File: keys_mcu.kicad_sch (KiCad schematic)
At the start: 30 parts, among them J3 Conn_01x26_Socket, J5 Conn_ARM_JTAG_SWD_10, J6 Conn_02x03_Odd_Even, SW1 PWR, SW2 MUTE, SW2 Volume, SW3 PREV, SW4 PLAY_PAUSE, SW5 NEXT, U2 STM32G431CBUx, U7 SN65HVD230

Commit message: routing progress
Just nice to make some save points every now and again.
USB seems... ok?  Still need to check 3v3 or 5v on the power pullups,
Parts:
- added C2: 100nF, Capacitor_SMD:C_0603_1608Metric, symbol Device:C_Small
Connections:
- net +3V3: now also C2.2
- net GND: now also C2.1
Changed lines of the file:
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@@
   (junction (at 226.06 144.78) (diameter 0) (color 0 0 0 0)
+  )
+  (junction (at 203.2 63.5) (diameter 0) (color 0 0 0 0)
   )
   (junction (at 236.22 30.48) (diameter 0) (color 0 0 0 0)
@@
     (stroke (width 0) (type default))
   )
+  (wire (pts (xy 223.52 63.5) (xy 223.52 66.04))
+    (stroke (width 0) (type default))
+  )
   (wire (pts (xy 264.16 48.26) (xy 269.24 48.26))
     (stroke (width 0) (type default))
@@
     (stroke (width 0) (type default))
   )
+  (wire (pts (xy 218.44 63.5) (xy 223.52 63.5))
+    (stroke (width 0) (type default))
+  )
   (wire (pts (xy 68.58 121.92) (xy 63.5 121.92))
     (stroke (width 0) (type default))
@@
   )
   (wire (pts (xy 203.2 63.5) (xy 203.2 66.04))
+    (stroke (width 0) (type default))
+  )
+  (wire (pts (xy 213.36 63.5) (xy 203.2 63.5))
     (stroke (width 0) (type default))
   )
@@
         (path "/d0e4eaec-96cb-4a0e-a384-5b3e3f5f8d5d/7c81bc9d-f306-4c7f-90ce-10f7b22818e4"
           (reference "D3") (unit 1)
+        )
+      )
+    )
+  )
+  (symbol (lib_id "power:GND") (at 223.52 66.04 0) (unit 1)
+    (in_bom yes) (on_board yes) (dnp no) (fields_autoplaced)
+    (property "Reference" "#PWR047" (at 223.52 72.39 0)
+      (effects (font (size 1.27 1.27)) hide)
+    )
+    (property "Value" "GND" (at 223.52 71.12 0)
+      (effects (font (size 1.27 1.27)))
+    )
+    (property "Footprint" "" (at 223.52 66.04 0)
+      (effects (font (size 1.27 1.27)) hide)
+    )
+    (property "Datasheet" "" (at 223.52 66.04 0)
+      (effects (font (size 1.27 1.27)) hide)
+    )
+    (pin "1")
+    (instances
+      (project "das-kb4-bara2"
+        (path "/d0e4eaec-96cb-4a0e-a384-5b3e3f5f8d5d/7c81bc9d-f306-4c7f-90ce-10f7b22818e4"
+          (reference "#PWR047") (unit 1)
         )
       )
@@
         )
       )
+    )
+  )
+  (symbol (lib_id "Device:C_Small") (at 215.9 63.5 270) (unit 1)
+    (in_bom yes) (on_board yes) (dnp no)
+    (property "Reference" "C2" (at 214.6236 60.96 0)
+      (effects (font (size 1.27 1.27)) (justify right))
+    )
+    (property "Value" "100nF" (at 218.44 63.5 0)
+      (effects (font (size 1.27 1.27)) (justify right))
+    )
+    (property "Footprint" "Capacitor_SMD:C_0603_1608Metric" (at 215.9 63.5 0)
+      (effects (font (size 1.27 1.27)) hide)
+    )
+    (property "Datasheet" "~" (at 215.9 63.5 0)
+      (effects (font (size 1.27 1.27)) hide)
+    )
+    (property "MPN" "CC0603KRX7R9BB104 " (at 215.9 63.5 0)
+      (effects (font (size 1.27 1.27)) hide)
+    )
+    (property "lcsc#" "C14663" (at 215.9 63.5 0)
+      (effects (font (size 1.27 1.27)) hide)
+    )
+    (property "jlc-basic" "1" (at 215.9 63.5 0)
+      (effects (font (size 1.27 1.27)) hide)
+    )
+    (property "lcsc2#" "" (at 215.9 63.5 0)
+      (effects (font (size 1.27 1.27)) hide)
+    )
+    (pin "1")
+    (pin "2")
+    (instances
+      (project "r2022-12"
+        (path "/9d3292e9-89ed-435a-b615-fc52a41b2a3d/00000000-0000-0000-0000-00005e1ad3c1"
+          (reference "C2") (unit 1)
+        )
+      )
+      (project "das-kb4-bara2"
+        (path "/d0e4eaec-96cb-4a0e-a384-5b3e3f5f8d5d/f457a5c4-270e-459d-a4f0-150cf90e3909"
+          (reference "C1") (unit 1)
+        )
+        (path "/d0e4eaec-96cb-4a0e-a384-5b3e3f5f8d5d/7c81bc9d-f306-4c7f-90ce-10f7b22818e4"
+          (reference "C15") (unit 1)
+        )
+      )

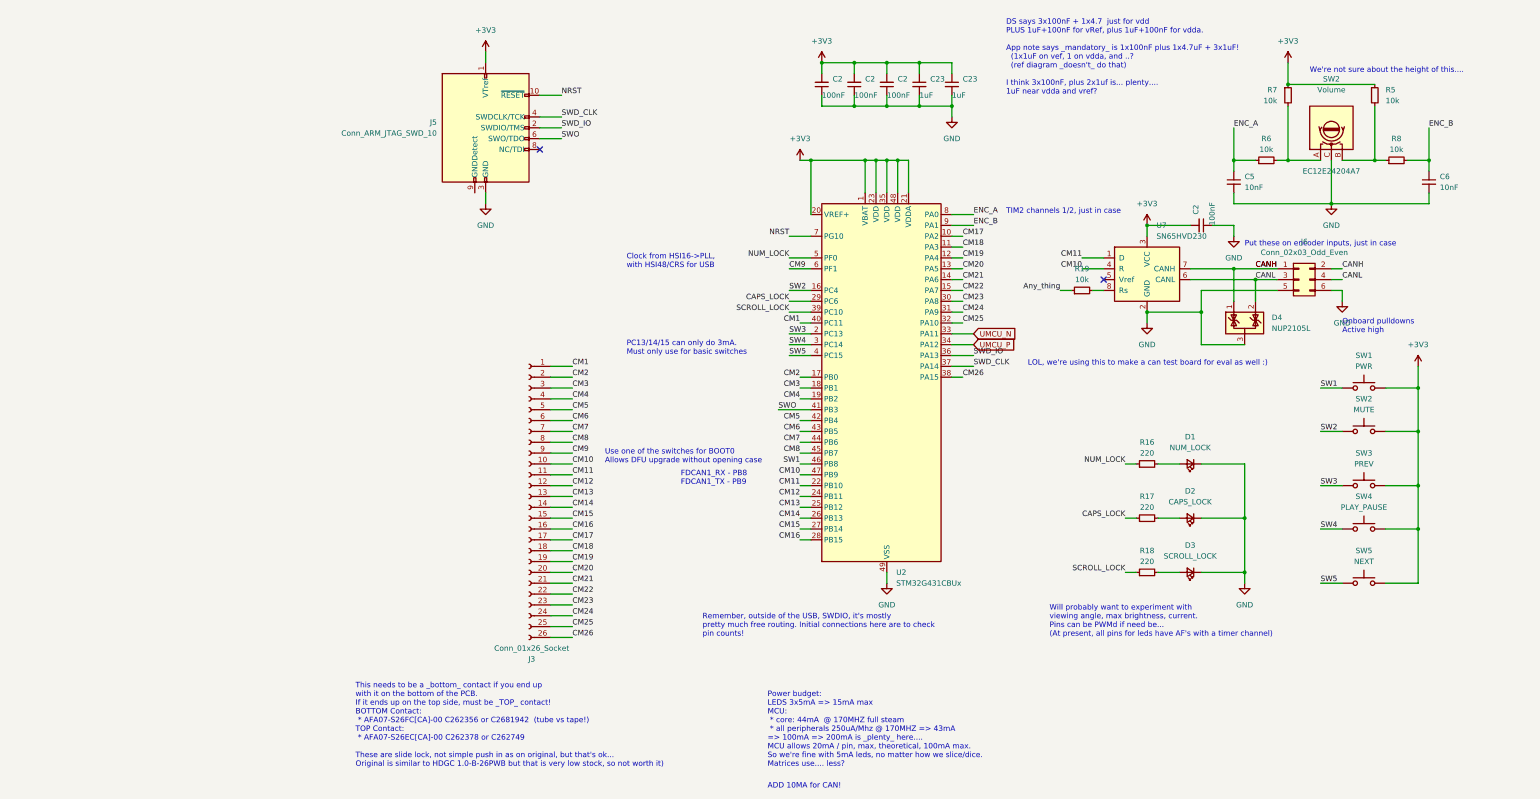
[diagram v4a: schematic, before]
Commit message: cleanup schematic, break out most of it
Broke it all out to the right places, now I can go and shuffle all the
labels to make it line up.  Thankfully we can just "freely" route the
keybaord matrix pins!
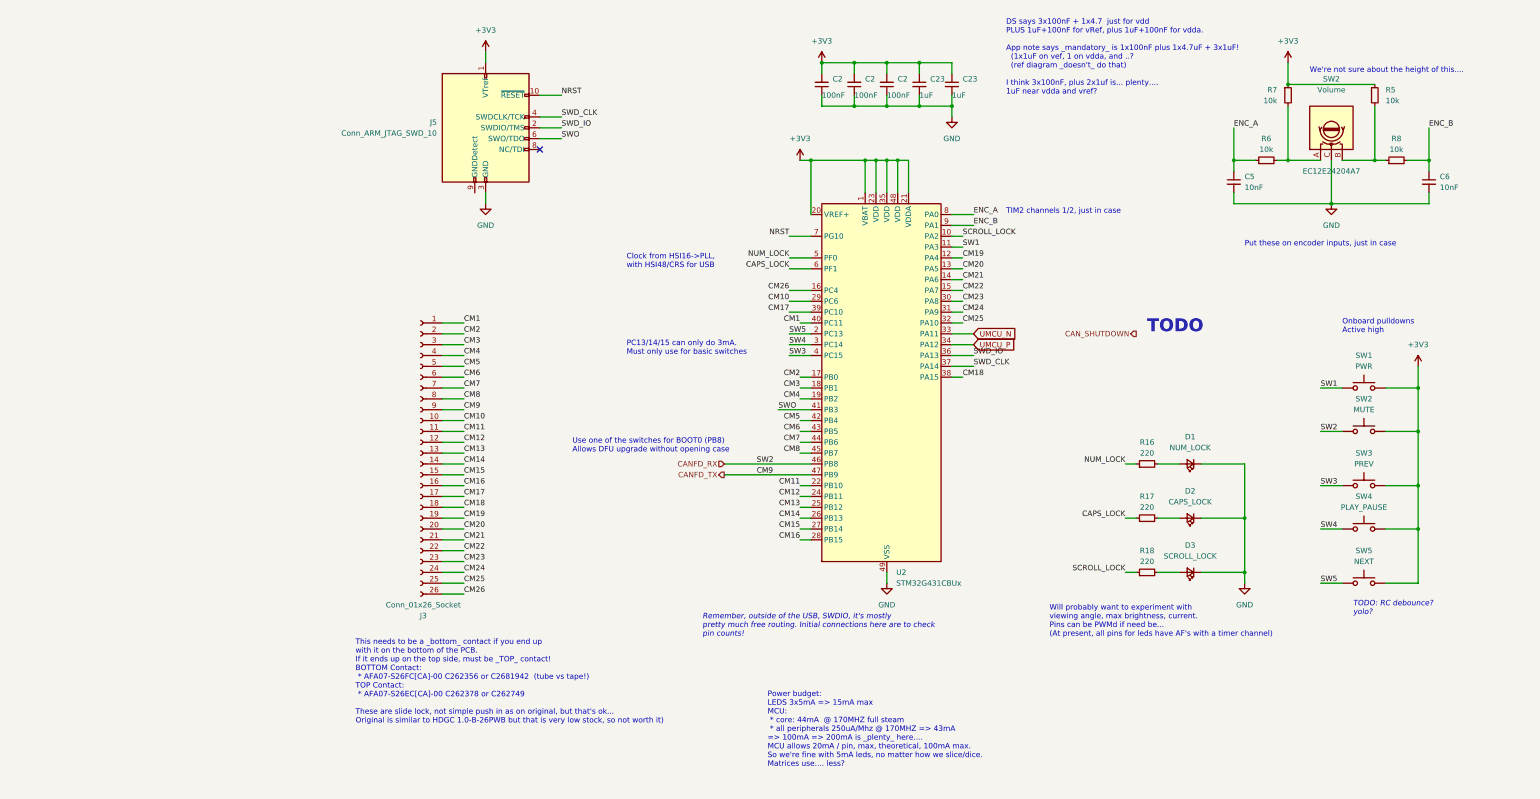
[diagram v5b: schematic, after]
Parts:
- removed C2: 100nF, Capacitor_SMD:C_0603_1608Metric, symbol Device:C_Small
- removed D4: NUP2105L, Package_TO_SOT_SMD:SOT-23, symbol Power_Protection:NUP2105L
- removed J6: Conn_02x03_Odd_Even, Connector_PinHeader_2.54mm:PinHeader_2x03_P2.54mm_Vertical, symbol Connector_Generic:Conn_02x03_Odd_Even
- removed R19: 10k, Resistor_SMD:R_0603_1608Metric, symbol Device:R_Small
- removed U7: SN65HVD230, Package_SO:SOIC-8_3.9x4.9mm_P1.27mm, symbol Interface_CAN_LIN:SN65HVD230
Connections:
- net CAPS_LOCK: now also U2.6 (PF1); no longer U2.29 (PC6)
- net CM10: now also U2.29 (PC6); no longer U2.47 (PB9)
- net CM17: now also U2.39 (PC10); no longer U2.10 (PA2)
- net CM18: now also U2.38 (PA15); no longer U2.11 (PA3)
- net CM26: now also U2.16 (PC4); no longer U2.38 (PA15)
- net SCROLL_LOCK: now also U2.10 (PA2); no longer U2.39 (PC10)
- net SW1: now also U2.11 (PA3); no longer U2.46 (PB8)
- net SW3: now also U2.4 (PC15); no longer U2.2 (PC13)
- net SW5: now also U2.2 (PC13); no longer U2.4 (PC15)
- net CM9 renamed CANFD_TX
- net CANFD_TX: now also U2.47 (PB9); no longer U2.6 (PF1)
- net SW2 renamed CANFD_RX
- net CANFD_RX: now also U2.46 (PB8); no longer U2.16 (PC4)
- no-connect marks 2 -> 1
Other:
- note added: "TODO"
- note added: "TODO: RC debounce? yolo?"
- note added: "Use one of the switches for BOOT0 (PB8) Allows DFU upgrade without opening case"
- note removed: "ADD 10MA for CAN!"
- note removed: "FDCAN1_RX - PB8 FDCAN1_TX - PB9"
- note removed: "LOL, we're using this to make a can test board for eval as well :)"
- note removed: "Use one of the switches for BOOT0 Allows DFU upgrade without opening case"
- company: (none) -> Ekta Labs
- title: (none) -> Das KB4-Bara2
- moved on the sheet: J3
